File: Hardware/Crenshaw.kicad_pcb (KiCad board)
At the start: 2 copper layers, 41 x 23.7 mm, 24 parts, among them J1 Jumper_Voltage, J2 I2C, J3 I2C, P1 SSD1306_ribbon, U1 AP2112K-3.3

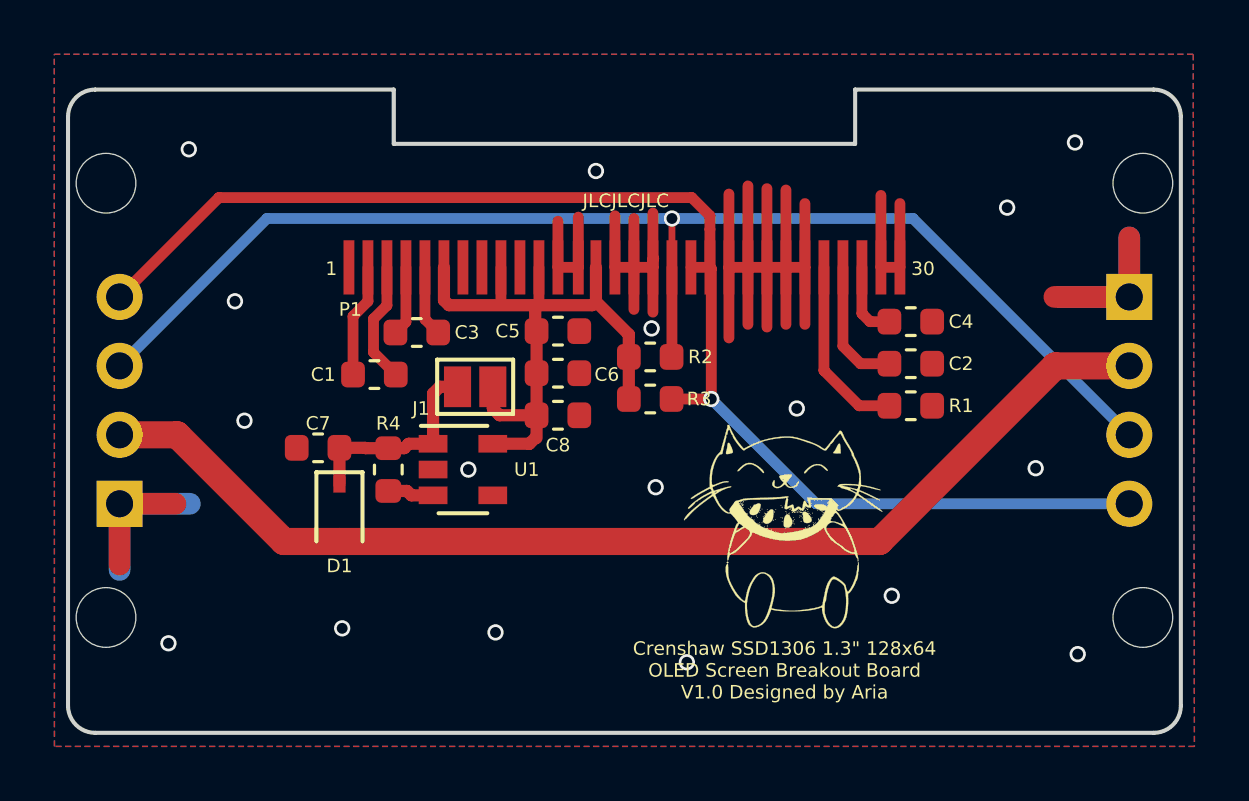
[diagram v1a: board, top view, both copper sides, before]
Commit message: SOD323 schottky switched to SOD123
Bigger means less heat issues
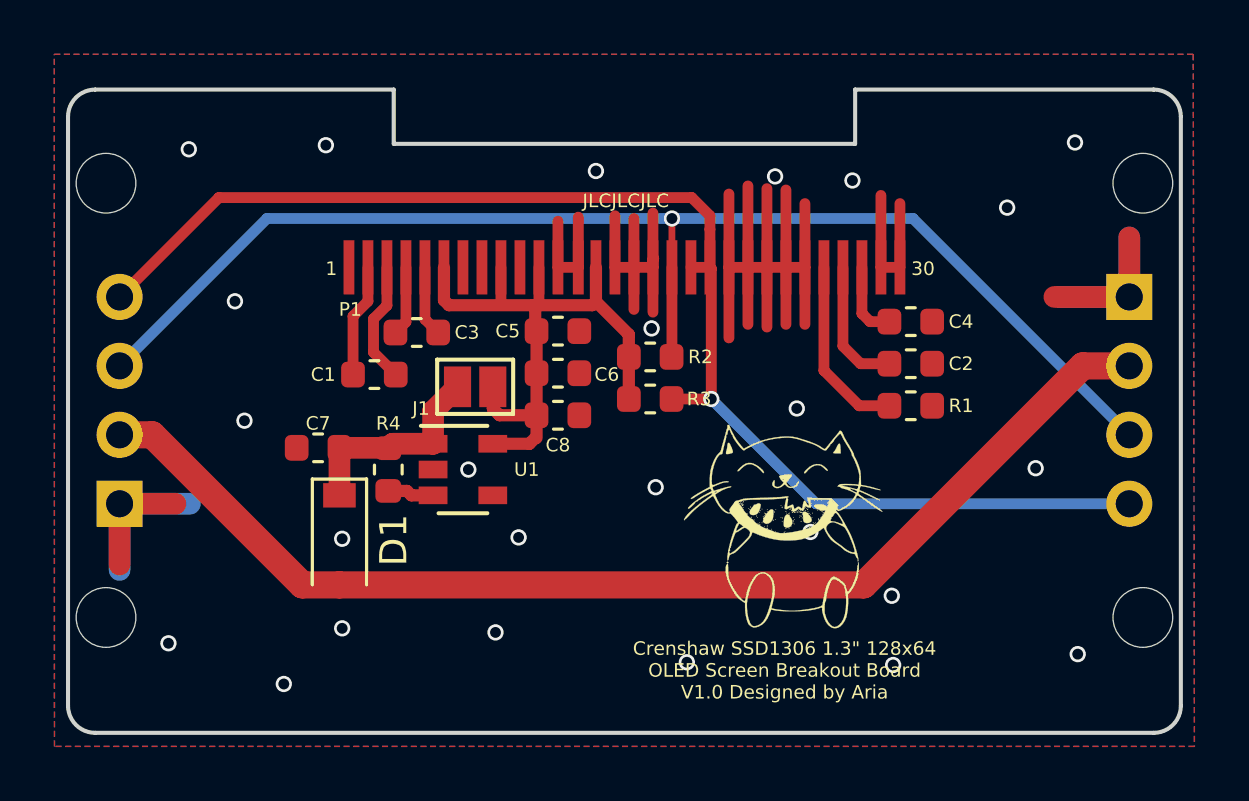
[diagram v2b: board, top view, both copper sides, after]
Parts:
- D1: footprint Diode_SMD:D_SOD-323 -> Diode_SMD:D_SOD-123
- J2, J3: footprint Custom Parts:PinHeader_1x04_P2.54mm_Vertical_No_Silk -> Crenshaw:PinHeader_1x04_P2.54mm_Vertical_No_Silk
- P1: footprint Custom Parts:SSD1306_ribbon -> Crenshaw:SSD1306_ribbon
- moved D1 1.00 mm to (171.5, 116.4)
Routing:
- net Net-(D1-Pad2): track 41.5 -> 42.8 mm
- net GND: vias 17 -> 25

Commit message: Updated to V1.1 - fixed several major errors
Fixed issue with orientation of I2C headers, increased size of silkscreen text, and moved ribbon cable connector lower down the board.
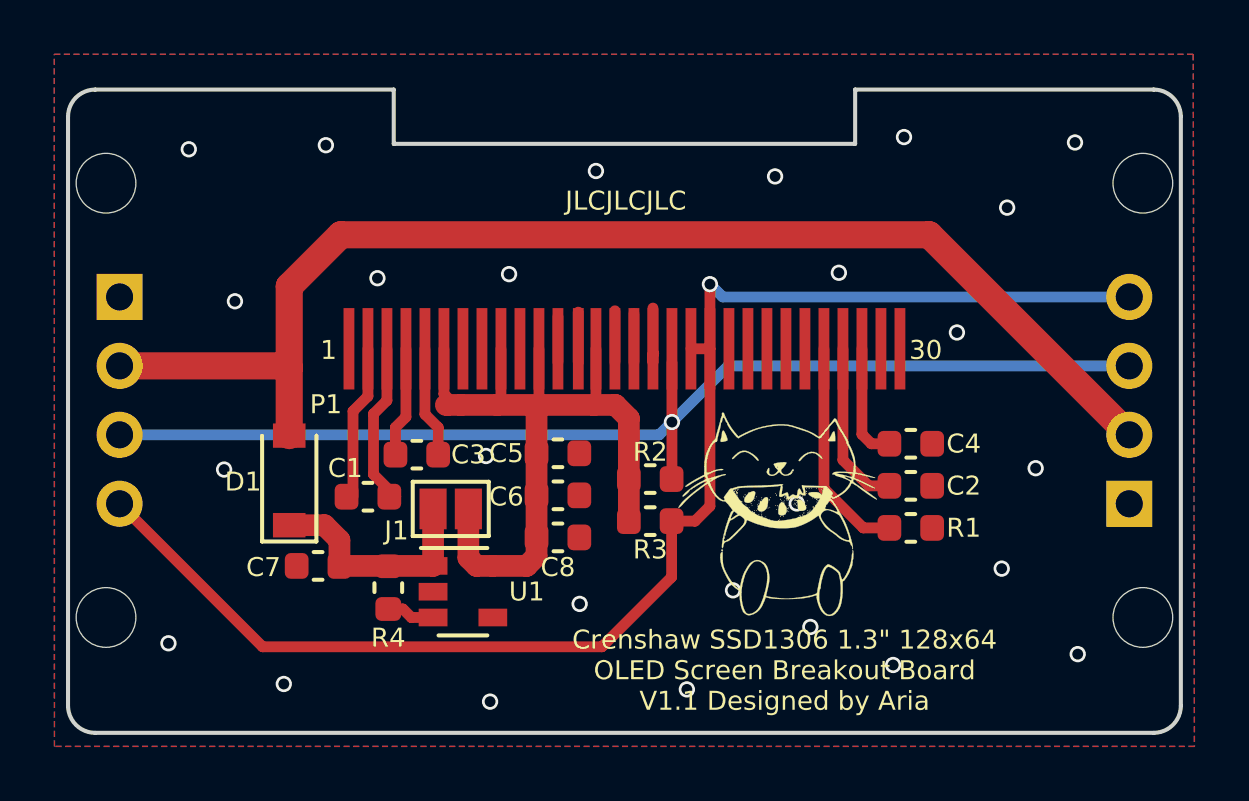
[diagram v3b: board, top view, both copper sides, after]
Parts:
- moved J1 4.59 mm to (175.6, 115.2)
- moved C1 4.51 mm to (172.6, 114.8)
- moved C2 4.50 mm to (192.6, 114.4)
- moved C3 4.50 mm to (174.3, 113.2)
- moved C4 4.50 mm to (192.6, 112.9)
- moved C5 4.50 mm to (179.6, 113.2)
- moved C6 4.50 mm to (179.5, 114.7)
- moved C8 4.50 mm to (179.6, 116.3)
- moved R1 4.50 mm to (192.6, 116.0)
- moved R2 4.50 mm to (182.9, 114.2)
- moved R3 4.50 mm to (182.9, 115.7)
- moved U1 4.50 mm to (176.1, 118.3)
- moved C7 4.35 mm to (170.7, 117.3)
- moved R4 4.35 mm to (173.3, 118.2)
- moved P1 3.00 mm to (182.0, 109.3)
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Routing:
- net GND: track 67.5 -> 9.64 mm, vias 25 -> 26
- net SDA: track 60.0 -> 51.8 mm
- net VDD: track 23.9 -> 29.7 mm
- net SCL: track 47.9 -> 42.6 mm
- net Net-(D1-Pad2): track 42.8 -> 46.6 mm
- net Net-(C3-Pad2): track 2.56 -> 4.06 mm
- net Net-(C3-Pad1): track 2.60 -> 4.10 mm
- net Net-(C1-Pad2): track 4.18 -> 5.68 mm
- net Net-(C1-Pad1): track 4.49 -> 5.99 mm
- net Net-(C4-Pad2): track 2.84 -> 4.31 mm
- net Net-(P1-Pad26): track 6.75 -> 8.16 mm
- net Net-(C2-Pad2): track 4.88 -> 6.21 mm
- net VCC: track 7.75 -> 8.58 mm
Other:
- board text added: "Crenshaw SSD1306 1.3" 128x64 OLED Screen Breakout Board V1.1 Designed by Aria"
- board text removed: "Crenshaw SSD1306 1.3" 128x64 OLED Screen Breakout Board V1.0 Designed by Aria"

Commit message: Added renders and updated readme
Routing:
- net SDA: track 51.8 -> 52.8 mm
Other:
- board text removed: "JLCJLCJLC"

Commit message: Better render
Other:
- board text added: "Crenshaw V1.1 Aria"
- board text removed: "Crenshaw SSD1306 1.3" 128x64 OLED Screen Breakout Board V1.1 Designed by Aria"

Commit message: Updated to V1.2
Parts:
- moved P1 3.00 mm to (182.0, 106.3)
- moved C3 2.55 mm to (174.8, 110.8)
- moved C1 2.00 mm to (172.6, 112.8)
- moved C7 1.58 mm to (169.2, 117.8)
- moved C4 1.41 mm to (193.6, 111.8)
- moved C2 1.12 mm to (193.6, 113.9)
- moved R1 1.00 mm to (193.6, 116.0)
- moved R4 1.00 mm to (172.3, 118.2)
- moved C5 1.00 mm to (179.6, 112.2)
- moved G*** 0.71 mm to (188.7, 113.8)
- moved C6 0.50 mm to (179.5, 114.2)
- moved J1 0.50 mm to (175.6, 114.8)
- moved R2 0.50 mm to (182.9, 113.7)
- moved U1 0.50 mm to (175.6, 118.3)
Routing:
- net Net-(C3-Pad2): track 4.06 -> 8.46 mm
- net Net-(D1-Pad2): track 46.6 -> 50.9 mm
- net SDA: track 52.8 -> 56.7 mm
- net Net-(P1-Pad26): track 8.16 -> 11.2 mm
- net SCL: track 42.6 -> 45.6 mm
- net Net-(C2-Pad2): track 6.21 -> 8.79 mm, vias 0 -> 1
- net VDD: track 29.7 -> 31.7 mm
- net Net-(C4-Pad2): track 4.31 -> 6.19 mm
- net GND: track 9.64 -> 10.8 mm, vias 26 -> 21
- net Net-(C1-Pad2): track 5.68 -> 6.78 mm
- net VCC: track 8.58 -> 9.61 mm
- net Net-(C3-Pad1): track 4.10 -> 4.81 mm
- net Net-(R4-Pad2): track 1.78 -> 2.28 mm
- added copper zone on F.Cu, net VDD
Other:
- board size 41 x 23.7 mm -> 41 x 24.5 mm
- board text added: "Crenshaw V1.2 Aria"
- board text removed: "Crenshaw V1.1 Aria"
